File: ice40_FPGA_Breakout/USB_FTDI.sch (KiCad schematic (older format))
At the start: 48 parts

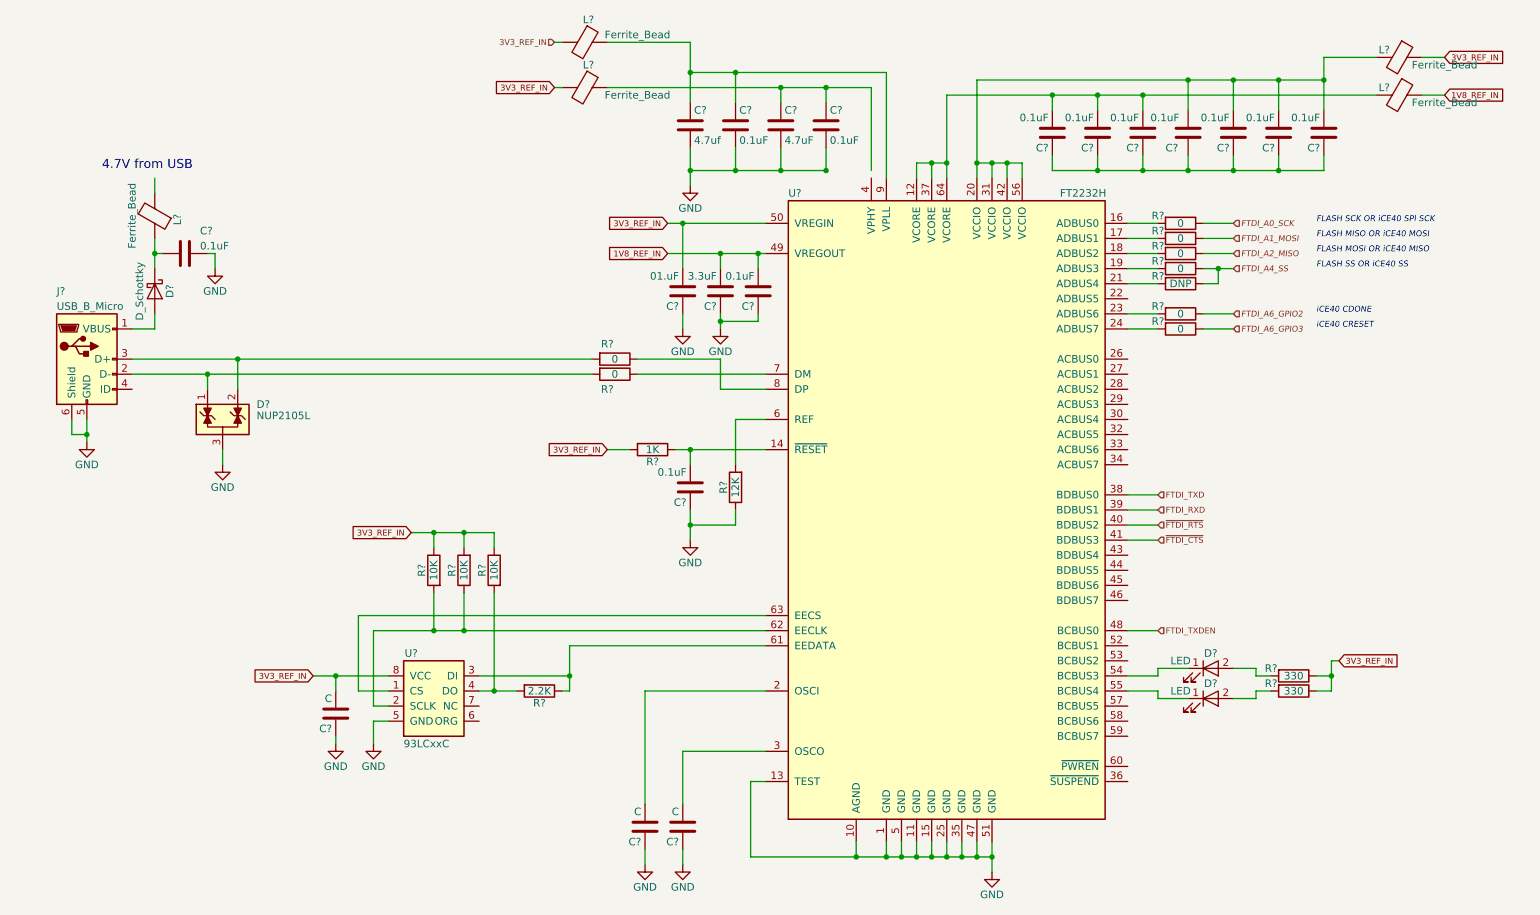
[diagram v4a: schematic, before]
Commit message: Add SPI EEPROM logic for SPI switching
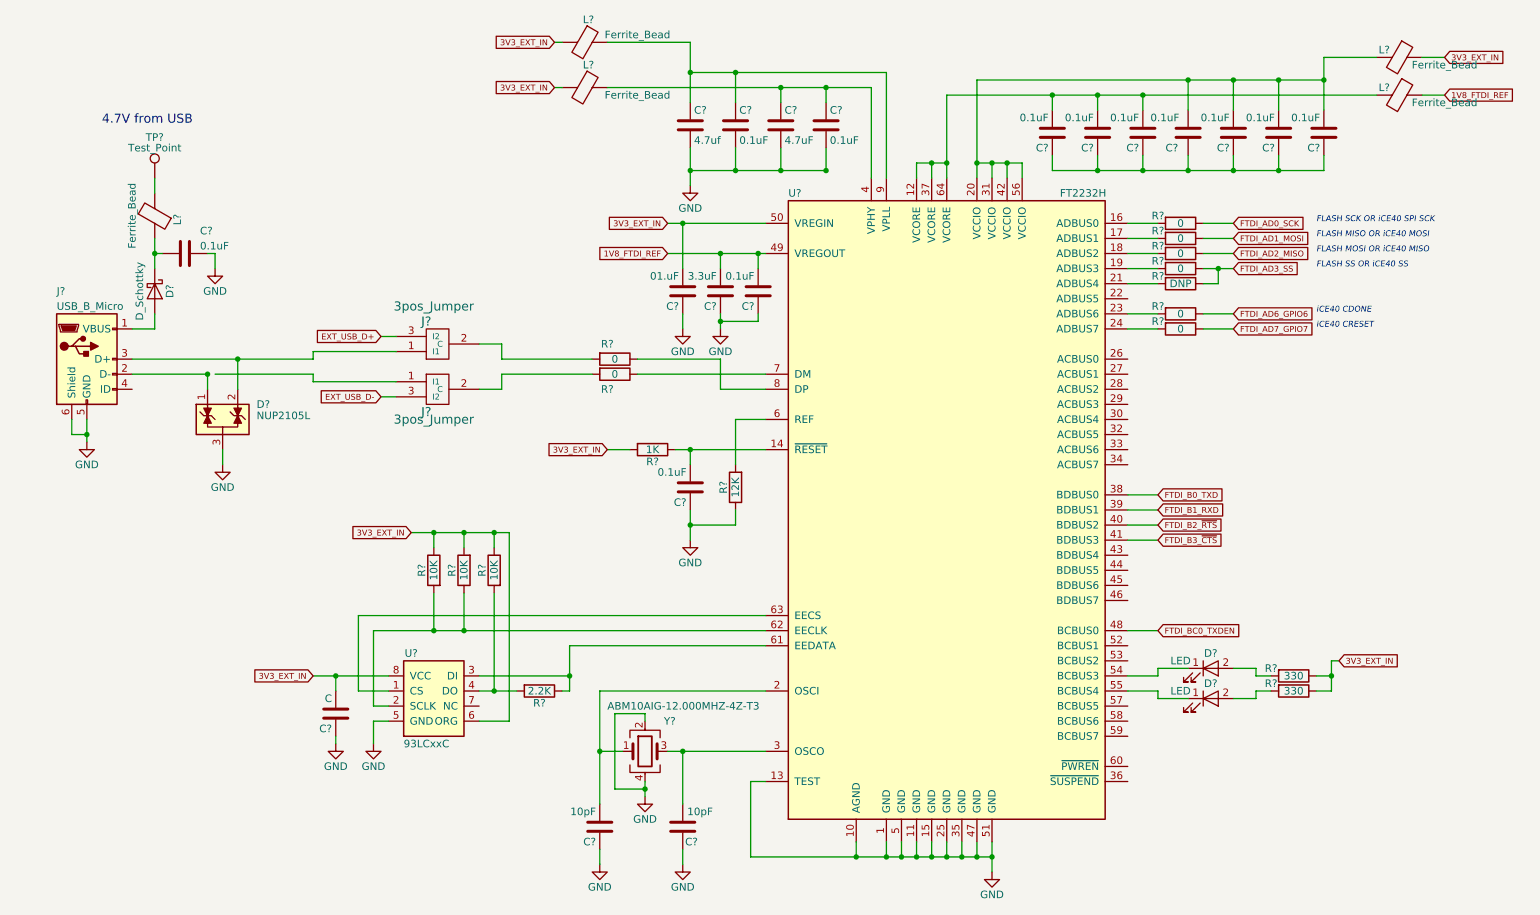
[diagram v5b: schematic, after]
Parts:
- added J? (x2): 3pos_Jumper, symbol 3pos_Jumper
- added TP?: Test_Point, symbol Test_Point
- added Y?: ABM10AIG-12.000MHZ-4Z-T3, symbol Crystal_GND24
- C? (x2): value C -> 10pF
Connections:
- net 3V3_REF_IN is gone; now on net 3V3_EXT_IN: C?.2, C?.2, L?.1, L?.2, L?.2, R?.1, R?.1, R?.1, R?.1, R?.2, R?.2, U?.50 (VREGIN), U?.8 (VCC)
- net GND: now also Y?.2, Y?.4
- net at D?.1 (K), J?.2 (D-): no longer R?.2
- net at D?.2 (K), J?.3 (D+): now also J?.1 (I1); no longer R?.2
- net at C?.1, C?.1, L?.1: now also U?.4 (VPHY)
- net at C?.2, U?.3 (OSCO): now also Y?.3
- net at C?.2, U?.2 (OSCI): now also Y?.1
- net at L?.2: now also TP?.1
- net 3V3_EXT_IN: now reaches U?.6 (ORG)
- net 1V8_REF_IN renamed 1V8_FTDI_REF
- net FTDI_A0_SCK renamed FTDI_AD0_SCK
- net FTDI_A1_MOSI renamed FTDI_AD1_MOSI
- net FTDI_A2_MISO renamed FTDI_AD2_MISO
- net FTDI_A4_SS renamed FTDI_AD3_SS
- net FTDI_A6_GPIO2 renamed FTDI_AD6_GPIO6
- net FTDI_A6_GPIO3 renamed FTDI_AD7_GPIO7
- net FTDI_RXD renamed FTDI_B1_RXD
- net FTDI_TXD renamed FTDI_B0_TXD
- net FTDI_TXDEN renamed FTDI_BC0_TXDEN
- net ~FTDI_CTS renamed FTDI_B3_~CTS
- net ~FTDI_RTS renamed FTDI_B2_~RTS
- new net: J?.2 (C), R?.2 (x2)
- new net EXT_USB_D+: J?.3 (I2)
- new net EXT_USB_D-: J?.3 (I2)
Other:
- moved on the sheet: C?

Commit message: global nets changed to hierarchy net, interconnects updated
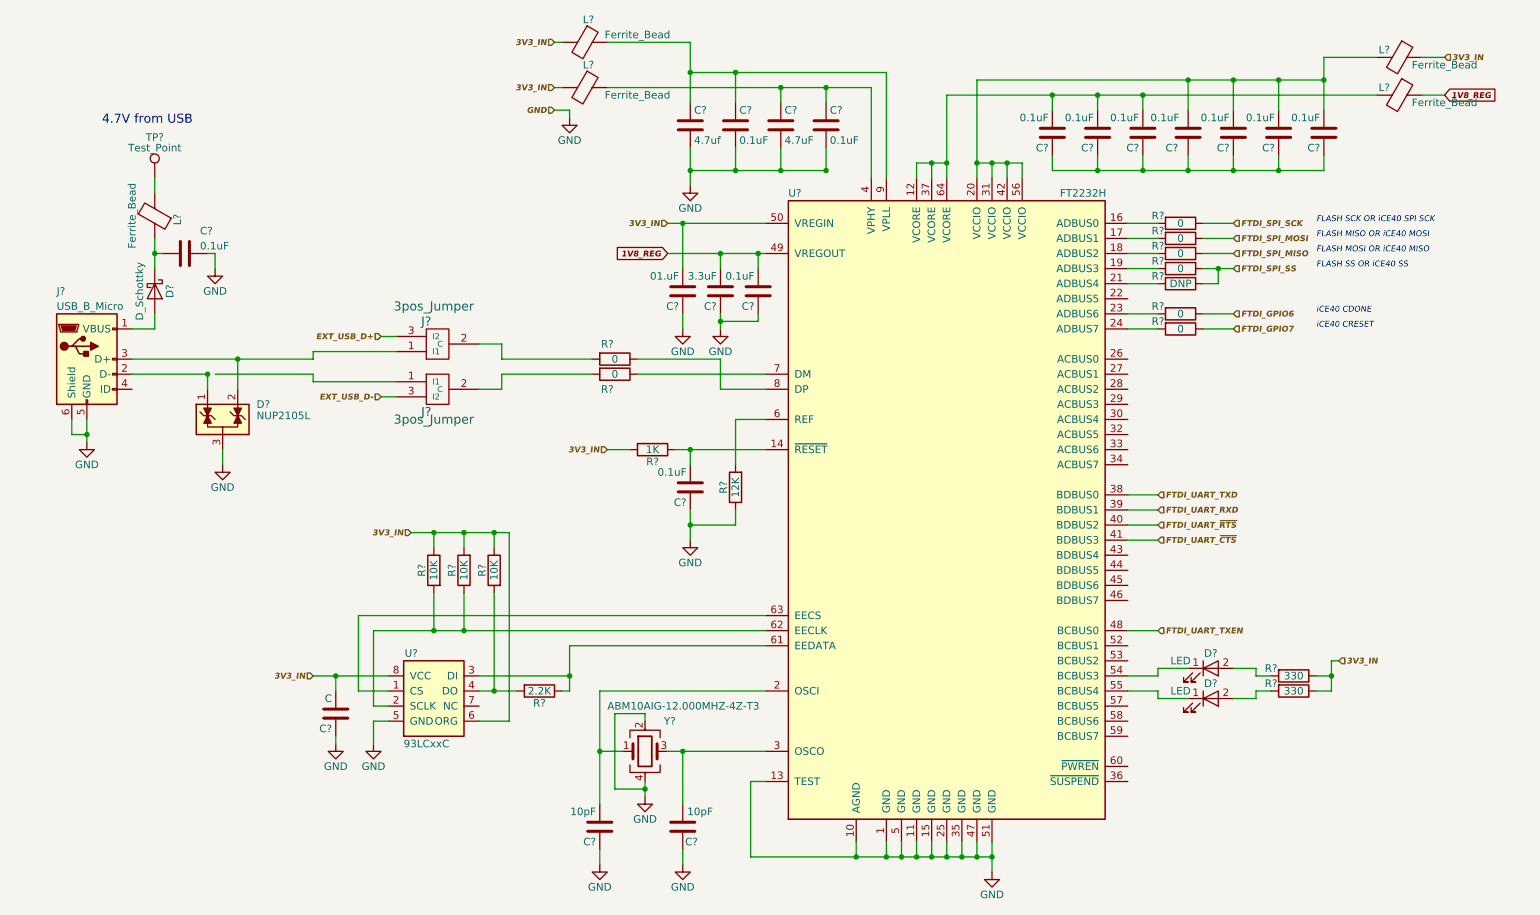
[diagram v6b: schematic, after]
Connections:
- net 1V8_FTDI_REF renamed 1V8_REG
- net 3V3_EXT_IN renamed 3V3_IN
- net FTDI_AD0_SCK renamed FTDI_SPI_SCK
- net FTDI_AD1_MOSI renamed FTDI_SPI_MOSI
- net FTDI_AD2_MISO renamed FTDI_SPI_MISO
- net FTDI_AD3_SS renamed FTDI_SPI_SS
- net FTDI_AD6_GPIO6 renamed FTDI_GPIO6
- net FTDI_AD7_GPIO7 renamed FTDI_GPIO7
- net FTDI_B0_TXD renamed FTDI_UART_TXD
- net FTDI_B1_RXD renamed FTDI_UART_RXD
- net FTDI_B2_~RTS renamed FTDI_UART_~RTS
- net FTDI_B3_~CTS renamed FTDI_UART_~CTS
- net FTDI_BC0_TXDEN renamed FTDI_UART_TXEN
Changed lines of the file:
@@
 $EndComp
 $Comp
-L GND #PWR02
+L GND #PWR019
 U 1 1 5A0D11EC
 P 7550 6150
-F 0 "#PWR02" H 7550 5900 50  0001 C CNN
+F 0 "#PWR019" H 7550 5900 50  0001 C CNN
 F 1 "GND" H 7550 6000 50  0000 C CNN
 F 2 "" H 7550 6150 50  0001 C CNN
@@
 $EndComp
 $Comp
-L GND #PWR03
+L GND #PWR020
 U 1 1 5A0D12CE
 P 5500 6100
-F 0 "#PWR03" H 5500 5850 50  0001 C CNN
+F 0 "#PWR020" H 5500 5850 50  0001 C CNN
 F 1 "GND" H 5500 5950 50  0000 C CNN
 F 2 "" H 5500 6100 50  0001 C CNN
@@
 $EndComp
 $Comp
-L GND #PWR04
+L GND #PWR021
 U 1 1 5A0D137A
 P 4950 6100
-F 0 "#PWR04" H 4950 5850 50  0001 C CNN
+F 0 "#PWR021" H 4950 5850 50  0001 C CNN
 F 1 "GND" H 4950 5950 50  0000 C CNN
 F 2 "" H 4950 6100 50  0001 C CNN
@@
 $EndComp
 $Comp
-L GND #PWR05
+L GND #PWR022
 U 1 1 5A0D14C2
 P 5750 2550
-F 0 "#PWR05" H 5750 2300 50  0001 C CNN
+F 0 "#PWR022" H 5750 2300 50  0001 C CNN
 F 1 "GND" H 5750 2400 50  0000 C CNN
 F 2 "" H 5750 2550 50  0001 C CNN
@@
 $EndComp
 $Comp
-L GND #PWR06
+L GND #PWR023
 U 1 1 5A0D1506
 P 5500 2550
-F 0 "#PWR06" H 5500 2300 50  0001 C CNN
+F 0 "#PWR023" H 5500 2300 50  0001 C CNN
 F 1 "GND" H 5500 2400 50  0000 C CNN
 F 2 "" H 5500 2550 50  0001 C CNN
@@
 $EndComp
 $Comp
-L GND #PWR07
+L GND #PWR024
 U 1 1 5A0D154A
 P 3200 5300
-F 0 "#PWR07" H 3200 5050 50  0001 C CNN
+F 0 "#PWR024" H 3200 5050 50  0001 C CNN
 F 1 "GND" H 3200 5150 50  0000 C CNN
 F 2 "" H 3200 5300 50  0001 C CNN
@@
 $EndComp
 $Comp
-L GND #PWR08
+L GND #PWR025
 U 1 1 5A0D172E
 P 2400 2150
-F 0 "#PWR08" H 2400 1900 50  0001 C CNN
+F 0 "#PWR025" H 2400 1900 50  0001 C CNN
 F 1 "GND" H 2400 2000 50  0000 C CNN
 F 2 "" H 2400 2150 50  0001 C CNN
@@
 $EndComp
 $Comp
-L GND #PWR09
+L GND #PWR026
 U 1 1 5A0D17DA
 P 2450 3450
-F 0 "#PWR09" H 2450 3200 50  0001 C CNN
+F 0 "#PWR026" H 2450 3200 50  0001 C CNN
 F 1 "GND" H 2450 3300 50  0000 C CNN
 F 2 "" H 2450 3450 50  0001 C CNN
@@
 $EndComp
 $Comp
-L GND #PWR010
+L GND #PWR027
 U 1 1 5A0D263E
 P 1550 3300
-F 0 "#PWR010" H 1550 3050 50  0001 C CNN
+F 0 "#PWR027" H 1550 3050 50  0001 C CNN
 F 1 "GND" H 1550 3150 50  0000 C CNN
 F 2 "" H 1550 3300 50  0001 C CNN
@@
 $EndComp
 $Comp
-L GND #PWR011
+L GND #PWR028
 U 1 1 5A0E190F
 P 3450 5300
-F 0 "#PWR011" H 3450 5050 50  0001 C CNN
+F 0 "#PWR028" H 3450 5050 50  0001 C CNN
 F 1 "GND" H 3450 5150 50  0000 C CNN
 F 2 "" H 3450 5300 50  0001 C CNN
@@
 $EndComp
 $Comp
-L GND #PWR012
+L GND #PWR029
 U 1 1 5A0E83DE
 P 5550 3950
-F 0 "#PWR012" H 5550 3700 50  0001 C CNN
+F 0 "#PWR029" H 5550 3700 50  0001 C CNN
 F 1 "GND" H 5550 3800 50  0000 C CNN
 F 2 "" H 5550 3950 50  0001 C CNN
@@
 4.7V from USB
 $Comp
-L GND #PWR013
+L GND #PWR030
 U 1 1 5A0F5EF9
 P 5550 1600
-F 0 "#PWR013" H 5550 1350 50  0001 C CNN
+F 0 "#PWR030" H 5550 1350 50  0001 C CNN
 F 1 "GND" H 5550 1450 50  0000 C CNN
 F 2 "" H 5550 1600 50  0001 C CNN
@@
 Text Notes 9700 2550 0    39   Italic 0
 iCE40 CRESET
-Text GLabel 4650 950  0    39   Input ~ 0
-3V3_EXT_IN
-Text GLabel 5400 1850 0    39   Input ~ 0
-3V3_EXT_IN
-Text GLabel 5400 2050 0    39   Input ~ 0
-1V8_FTDI_REF
-Text GLabel 5000 3350 0    39   Input ~ 0
-3V3_EXT_IN
-Text GLabel 3700 3900 0    39   Input ~ 0
-3V3_EXT_IN
-Text GLabel 3050 4850 0    39   Input ~ 0
-3V3_EXT_IN
-Text GLabel 10550 750  2    39   Input ~ 0
-3V3_EXT_IN
-Text GLabel 10550 1000 2    39   Input ~ 0
-1V8_FTDI_REF
 $Comp
 L R R?
@@
 	1    0    0    -1
 $EndComp
-Text GLabel 9850 4750 2    39   Input ~ 0
-3V3_EXT_IN
-Text GLabel 4650 650  0    39   Input ~ 0
-3V3_EXT_IN
-Text GLabel 9150 1850 2    39   Input ~ 0
-FTDI_AD0_SCK
-Text GLabel 9150 1950 2    39   Input ~ 0
-FTDI_AD1_MOSI
-Text GLabel 9150 2050 2    39   Input ~ 0
-FTDI_AD2_MISO
-Text GLabel 9150 2150 2    39   Input ~ 0
-FTDI_AD3_SS
-Text GLabel 9150 2450 2    39   Input ~ 0
-FTDI_AD6_GPIO6
-Text GLabel 9150 2550 2    39   Input ~ 0
-FTDI_AD7_GPIO7
-Text GLabel 8650 3650 2    39   Input ~ 0
-FTDI_B0_TXD
-Text GLabel 8650 3750 2    39   Input ~ 0
-FTDI_B1_RXD
-Text GLabel 8650 3850 2    39   Input ~ 0
-FTDI_B2_~RTS
-Text GLabel 8650 3950 2    39   Input ~ 0
-FTDI_B3_~CTS
-Text GLabel 8650 4550 2    39   Input ~ 0
-FTDI_BC0_TXDEN
 Wire Wire Line
 	7550 5950 7550 6150
@@
 Connection ~ 5250 5600
 $Comp
-L GND #PWR?
+L GND #PWR031
 U 1 1 5A2C2E4B
 P 5250 5650
-F 0 "#PWR?" H 5250 5400 50  0001 C CNN
+F 0 "#PWR031" H 5250 5400 50  0001 C CNN
 F 1 "GND" H 5250 5500 50  0000 C CNN
 F 2 "" H 5250 5650 50  0001 C CNN
@@
 Wire Wire Line
 	3600 3000 3500 3000
-Text GLabel 3500 2600 0    39   Input ~ 0
-EXT_USB_D+
-Text GLabel 3500 3000 0    39   Input ~ 0
-EXT_USB_D-
 Wire Wire Line
 	4150 5150 4350 5150
@@
 	1    0    0    -1
 $EndComp
+Text HLabel 4650 650  0    39   Input Italic 8
+3V3_IN
+Text HLabel 4650 950  0    39   Input Italic 8
+3V3_IN
+Text HLabel 5000 3350 0    39   Input Italic 8
+3V3_IN
+Text HLabel 3700 3900 0    39   Input Italic 8
+3V3_IN
+Text HLabel 3050 4850 0    39   Input Italic 8
+3V3_IN
+Text HLabel 9850 4750 2    39   Input Italic 8
+3V3_IN
+Text HLabel 10550 750  2    39   Input Italic 8
+3V3_IN
+Text HLabel 8650 4550 2    39   Input Italic 8
+FTDI_UART_TXEN
+Text HLabel 8650 3650 2    39   Input Italic 8
+FTDI_UART_TXD
+Text HLabel 8650 3750 2    39   Input Italic 8
+FTDI_UART_RXD
+Text HLabel 8650 3850 2    39   Input Italic 8
+FTDI_UART_~RTS
+Text HLabel 8650 3950 2    39   Input Italic 8
+FTDI_UART_~CTS
+Text HLabel 9150 1850 2    39   Input Italic 8
+FTDI_SPI_SCK
+Text HLabel 9150 1950 2    39   Input Italic 8
+FTDI_SPI_MOSI
+Text HLabel 9150 2050 2    39   Input Italic 8
+FTDI_SPI_MISO
+Text HLabel 9150 2150 2    39   Input Italic 8
+FTDI_SPI_SS
+Text HLabel 9150 2450 2    39   Input Italic 8
+FTDI_GPIO6
+Text HLabel 9150 2550 2    39   Input Italic 8
+FTDI_GPIO7
+Text HLabel 3500 2600 0    39   Input Italic 8
+EXT_USB_D+
+Text HLabel 3500 3000 0    39   Input Italic 8
+EXT_USB_D-
+Text HLabel 5400 1850 0    39   Input Italic 8
+3V3_IN
+Text GLabel 10550 1000 2    39   Input Italic 8
+1V8_REG
+Text GLabel 5400 2050 0    39   Input Italic 8
+1V8_REG
+$Comp
+L GND #PWR032
+U 1 1 5A40997E
+P 4750 1150
+F 0 "#PWR032" H 4750 900 50  0001 C CNN
+F 1 "GND" H 4750 1000 50  0000 C CNN
+F 2 "" H 4750 1150 50  0001 C CNN
+F 3 "" H 4750 1150 50  0001 C CNN
+	1    4750 1150
+	1    0    0    -1
+$EndComp
+Text HLabel 4650 1100 0    39   Input Italic 8
+GND
+Wire Wire Line
+	4650 1100 4750 1100
+Wire Wire Line
+	4750 1100 4750 1150
 $EndSCHEMATC

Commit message: memory modules added
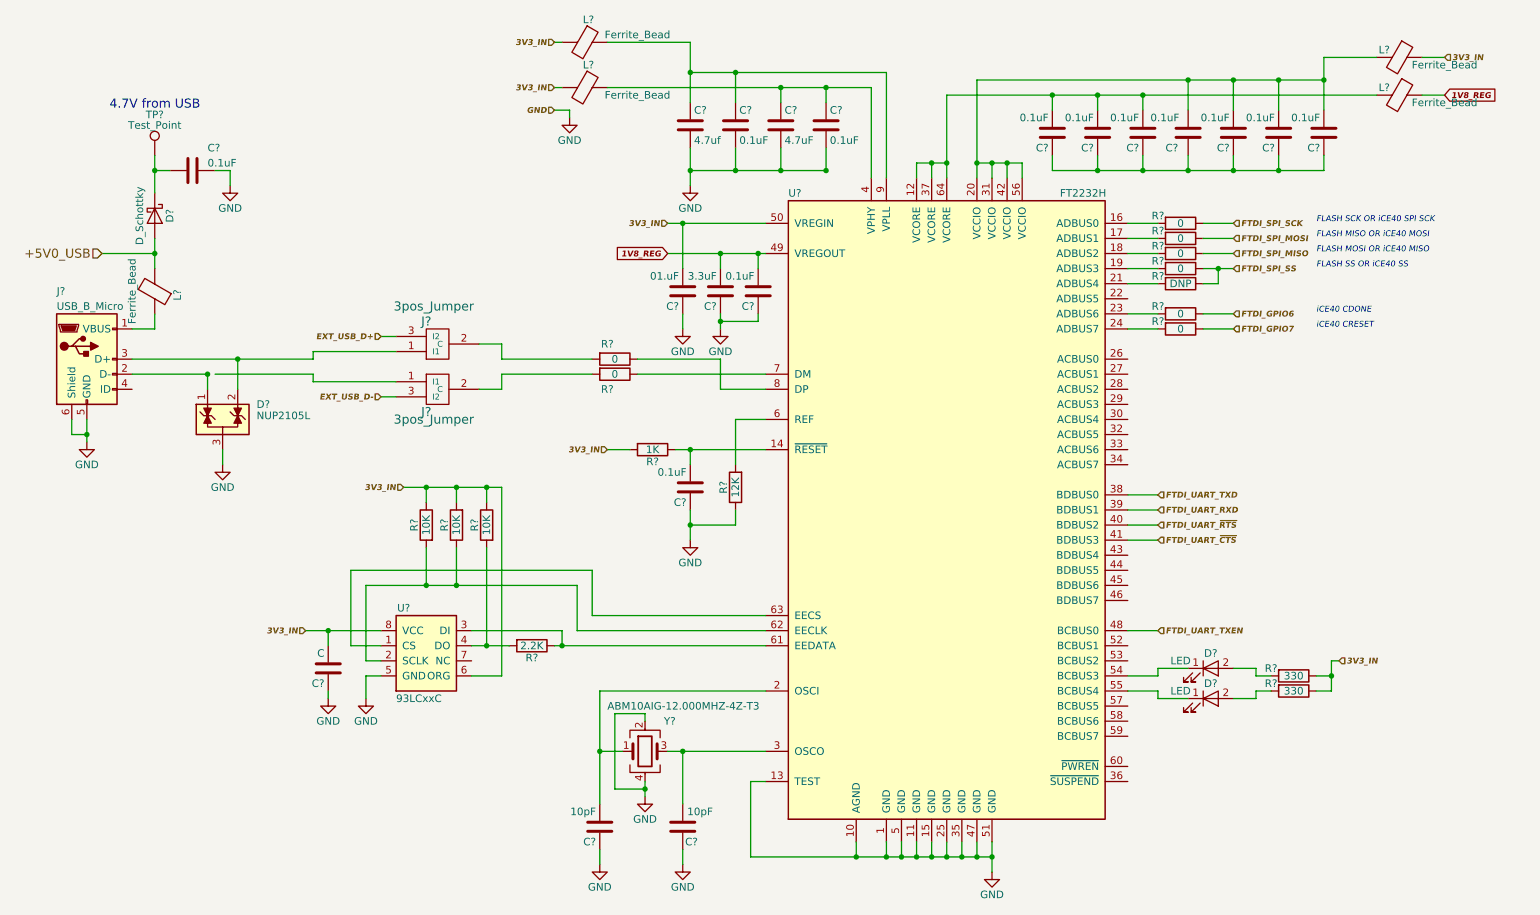
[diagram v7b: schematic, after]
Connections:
- net at J?.1 (VBUS): now also L?.1; no longer D?.2 (A)
- net at C?.2, D?.1 (K): now also TP?.1; no longer L?.1
- net +5V0_USB: now reaches L?.2
- net +5V0_USB: now also D?.2 (A); no longer TP?.1
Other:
- moved on the sheet: C?, D?, L?, R?, TP?, U?
